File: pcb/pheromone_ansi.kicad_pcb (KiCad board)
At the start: 2 copper layers, 304 x 99 mm, 160 parts, among them J1 USB_B_Micro, K1 KEYSW, K10 KEYSW, K11 KEYSW, K12 KEYSW, K13 KEYSW, K14 KEYSW, K15 KEYSW, K16 KEYSW, K17 KEYSW, K18 KEYSW, K19 KEYSW, K2 KEYSW, K20 KEYSW, K21 KEYSW, K22 KEYSW, K23 KEYSW, K24 KEYSW, K25 KEYSW, K26 KEYSW, K27 KEYSW, K28 KEYSW, K29 KEYSW, K3 KEYSW, K30 KEYSW, K31 KEYSW, K32 KEYSW, K33 KEYSW, K34 KEYSW, K35 KEYSW, K36 KEYSW, K37 KEYSW, K38 KEYSW, K39 KEYSW, K4 KEYSW, K40 KEYSW, K41 KEYSW, K42 KEYSW, K43 KEYSW, K44 KEYSW, K45 KEYSW, K46 KEYSW, K47 KEYSW, K48 KEYSW, K49 KEYSW, K5 KEYSW, K50 KEYSW, K51 KEYSW, K52 KEYSW, K53 KEYSW, K54 KEYSW, K55 KEYSW, K56 KEYSW, K57 KEYSW, K58 KEYSW, K59 KEYSW, K6 KEYSW, K60 KEYSW, K61 KEYSW, K62 KEYSW, K63 KEYSW, K7 KEYSW, K8 KEYSW, K9 KEYSW, P1 AVR-ISP-6, SW1 SW_PUSH, U1 ATMEGA32U4, Y1 Crystal_GND24

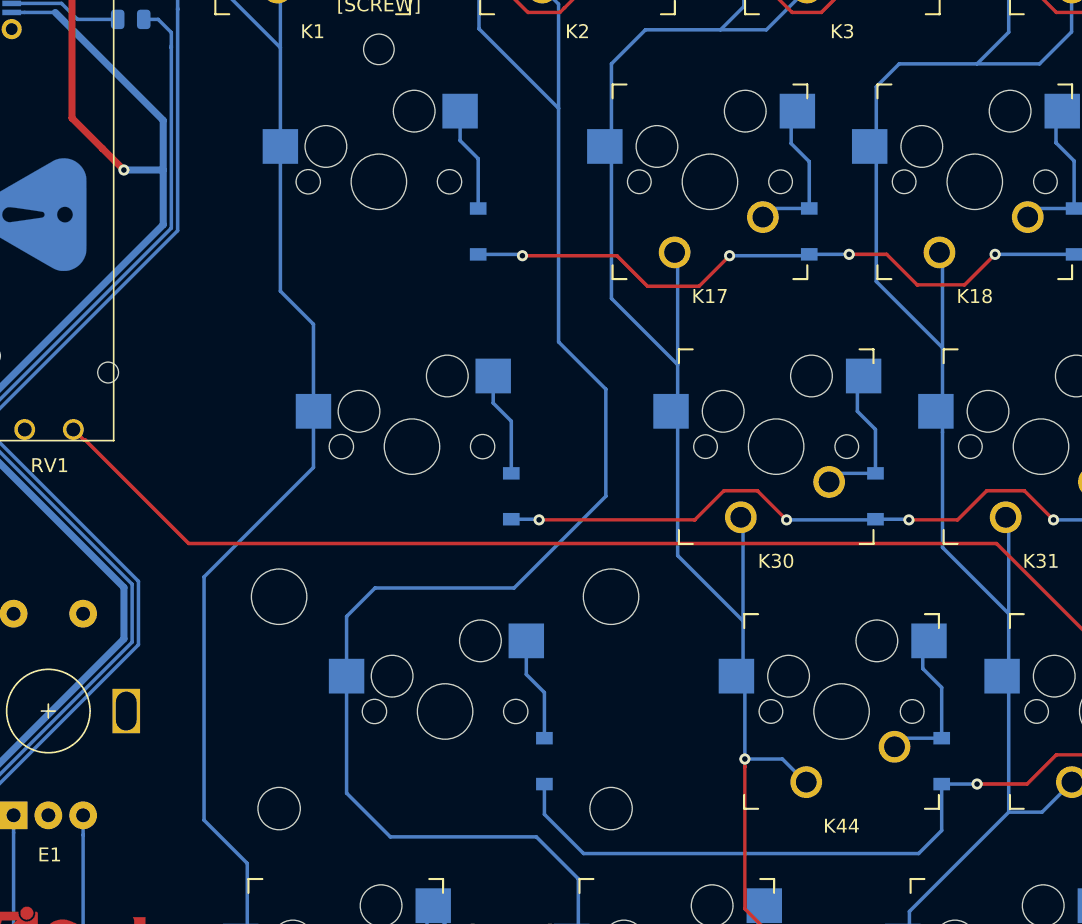
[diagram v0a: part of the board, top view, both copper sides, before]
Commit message: update some unmodified keys
update Tab, Caps Lock, and Left Shift footprints to hotswap optional
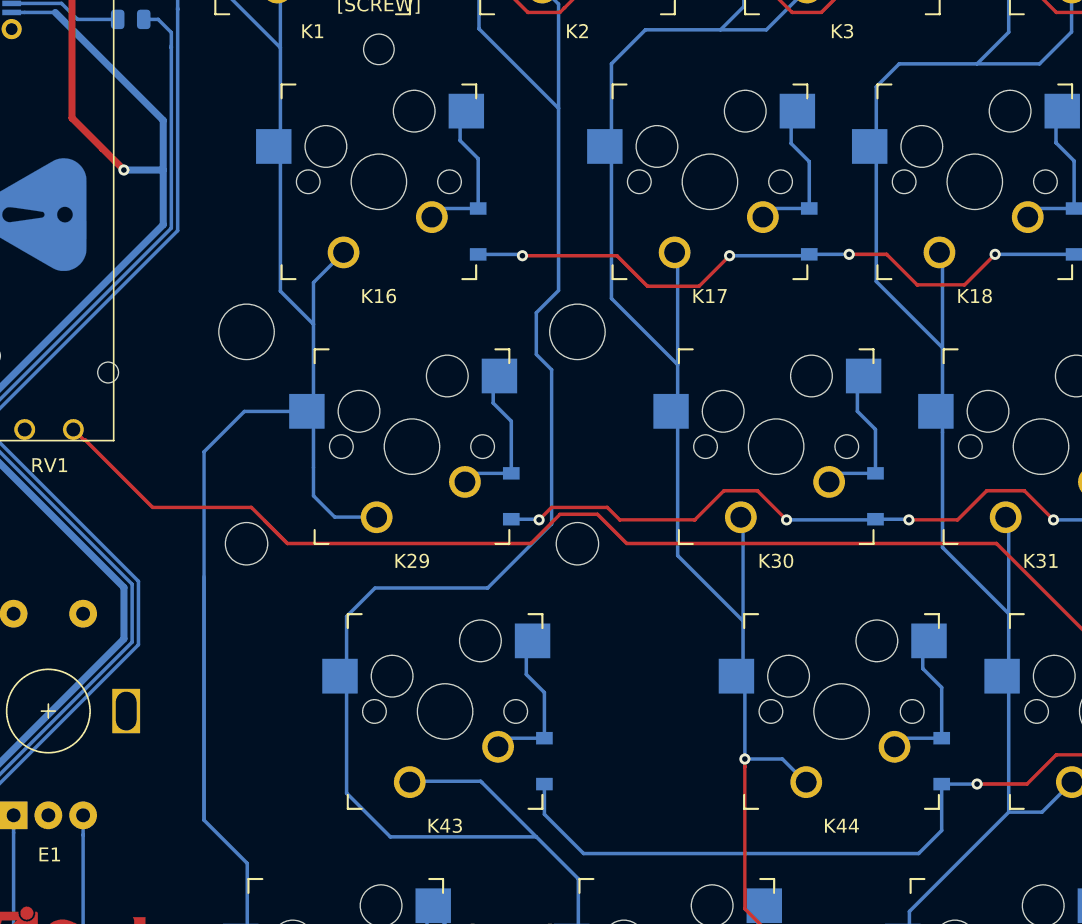
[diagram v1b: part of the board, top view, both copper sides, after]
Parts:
- added REF**: Stabilizer_MX_2u, keyswitches:Stabilizer_MX_2u, F.Cu at (69.1, 97.6)
- K16: footprint MX_Only:MXOnly-1.5U-Hotswap -> keyswitches:Kailh_socket_MX_optional
- K29: footprint MX_Only:MXOnly-1.75U-Hotswap -> keyswitches:Kailh_socket_MX_optional
- K43: footprint MX_Only:MXOnly-2U-Hotswap-ReversedStabilizers -> keyswitches:Kailh_socket_MX_optional
- turned K16 to 180 degrees
- turned K29 to 180 degrees
- turned K43 to 180 degrees
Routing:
- net COL0: track 205.7 -> 243.0 mm
- net COL1: track 209.9 -> 217.6 mm
- net ANALOG: track 143.5 -> 147.5 mm
- net Net-(D43-Pad2): track 7.54 -> 10.3 mm
- net Net-(D29-Pad2): track 7.54 -> 10.3 mm
- net Net-(D16-Pad2): track 7.54 -> 10.2 mm
- net SCK_ROW2: track 419.2 -> 420.0 mm

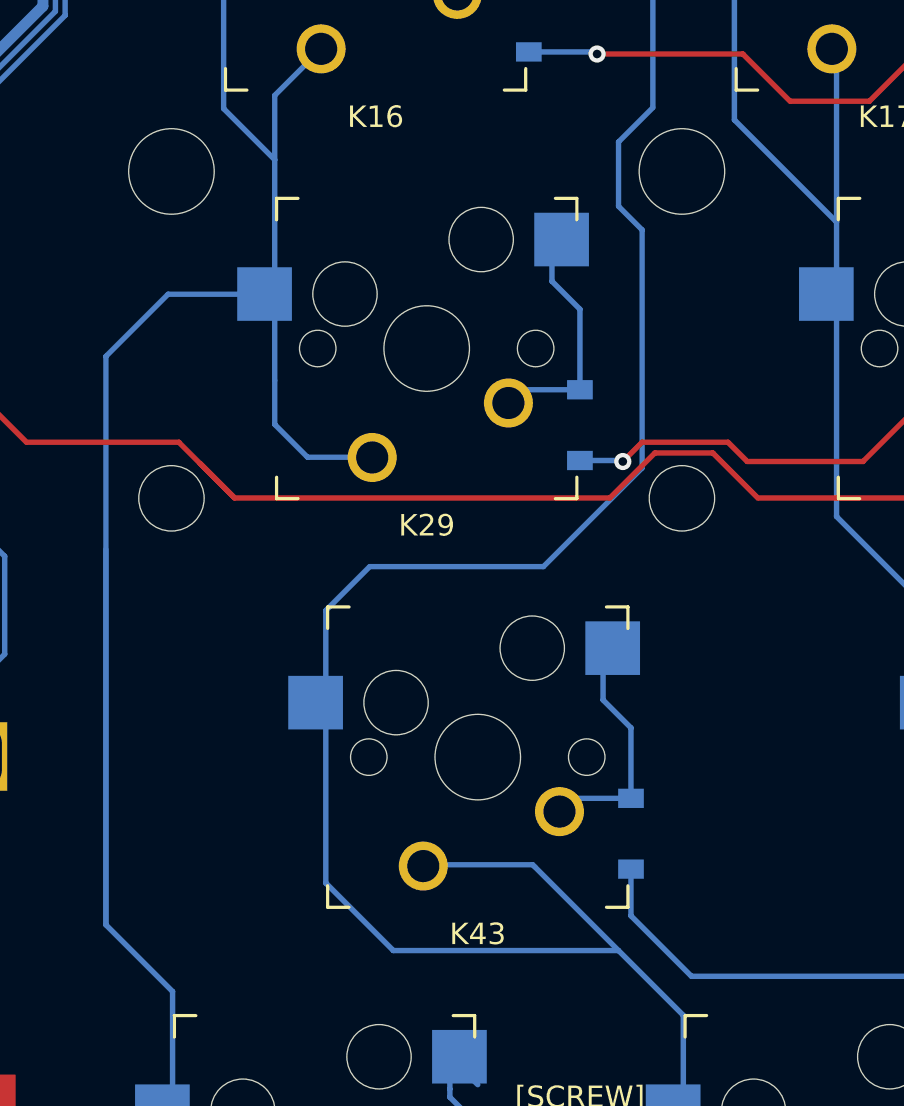
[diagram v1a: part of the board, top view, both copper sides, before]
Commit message: Fix left shift stabilizer placement
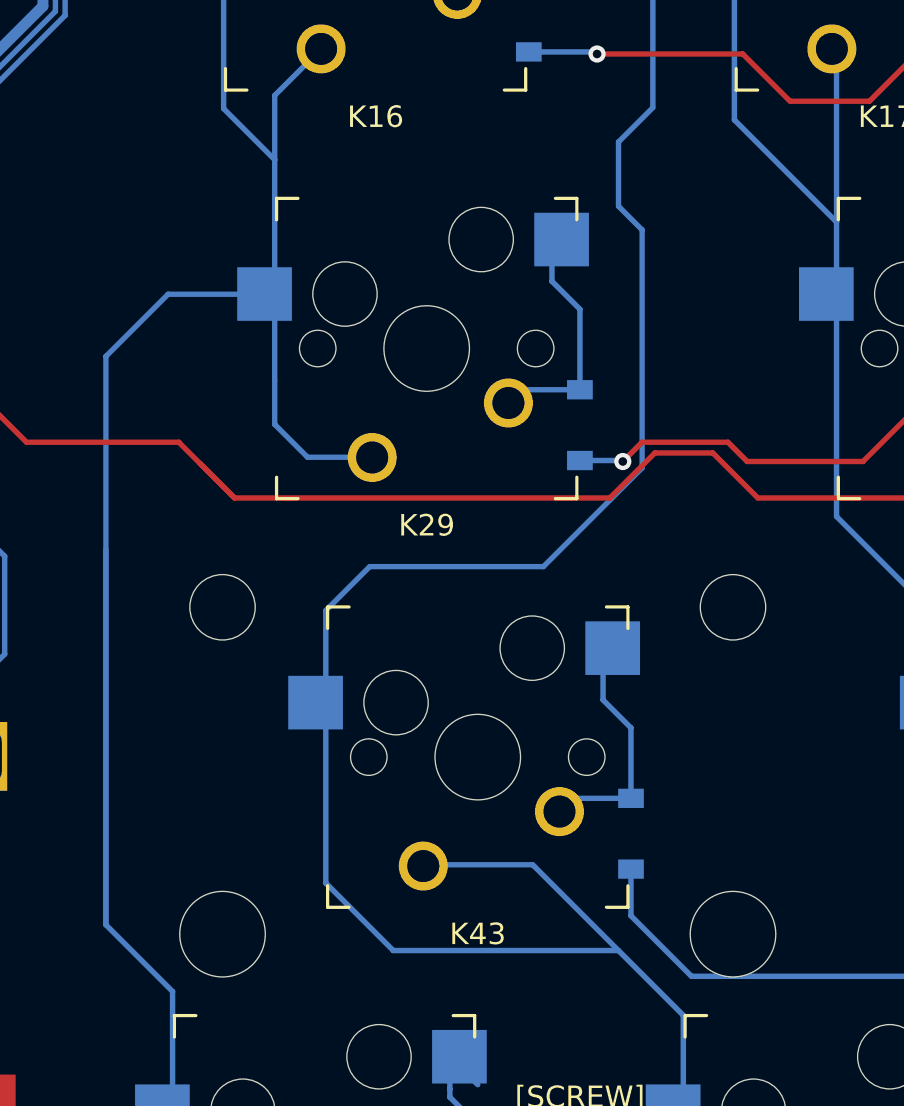
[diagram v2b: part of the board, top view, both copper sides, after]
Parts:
- moved REF** 19.2 mm to (71.4, 116.7), turned to 0 degrees
